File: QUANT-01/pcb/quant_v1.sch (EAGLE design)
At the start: 34 parts, among them SW1 SUBMINI_SPDT, SW2 SUBMINI_SPDT, SW3 SUBMINI_SPDT, SW4 SUBMINI_SPDT

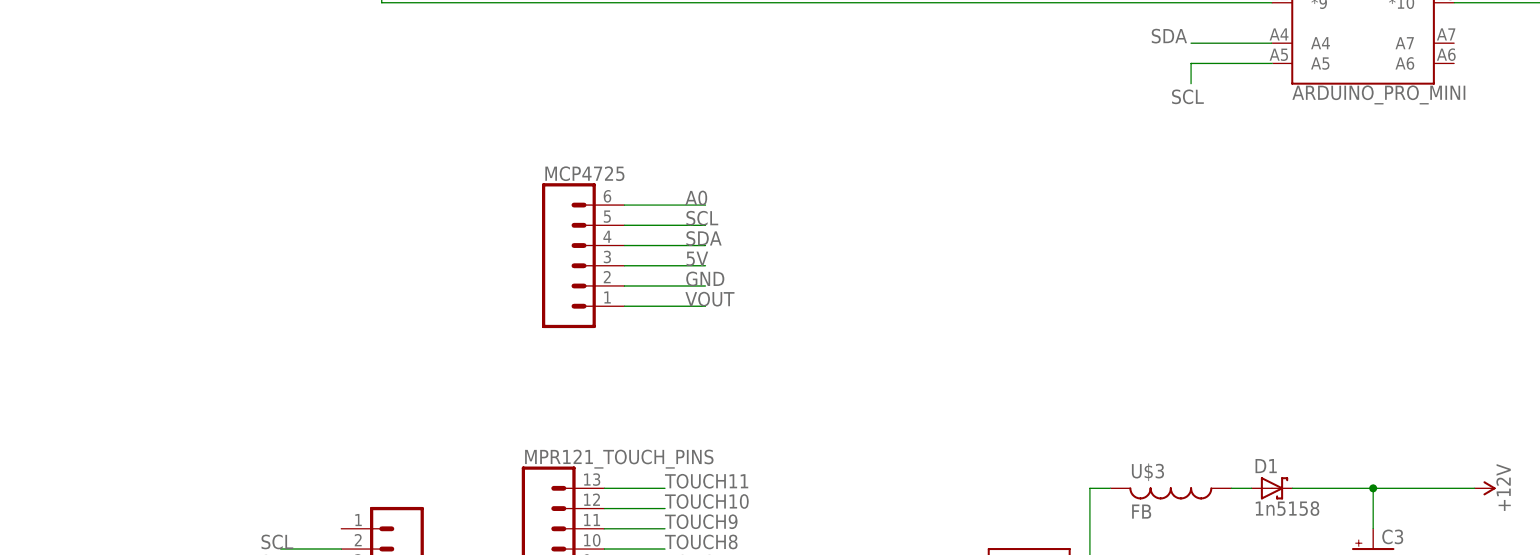
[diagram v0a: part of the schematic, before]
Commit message: added simple GATE out code.
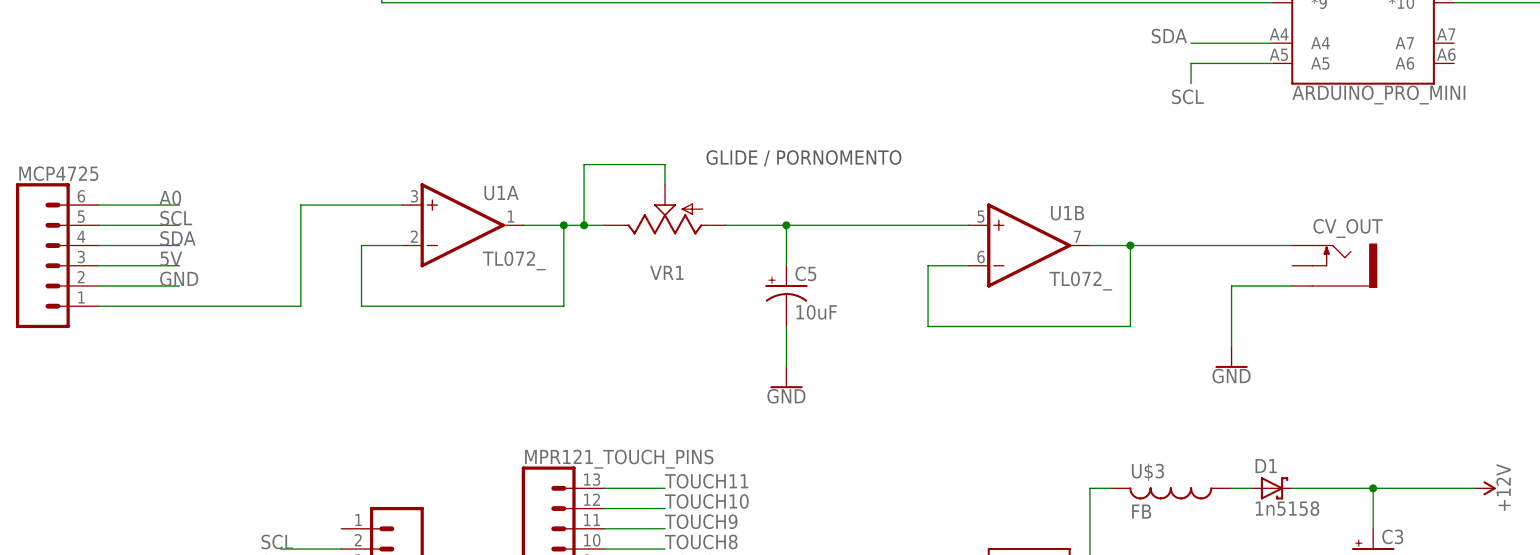
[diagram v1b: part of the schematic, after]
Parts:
- added C5: 10uF, SparkFun-Capacitors:10UF-POLAR-RADIAL-2.5MM-25V-20%
- added CV_OUT: THONKICONNNEW, MusicThingModular:THONKICONNNEW
- added U1: TL072_, MusicThingModular:TL072_
- added VR1: (no value), MusicThingModular:9MM_SNAP-IN_POT_
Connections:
- removed net VOUT: MCP4725.1
- new net N$20: MCP4725.1, U1A.+IN
- new net N$21: U1A.-IN, U1A.OUT, VR1.E, VR1.S
- new net N$23: C5.+, U1B.+IN, VR1.A
- new net N$25: CV_OUT.TIP, U1B.-IN, U1B.OUT
- net GND: now also C5.-, CV_OUT.SLEEVE
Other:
- note added: "GLIDE / PORNOMENTO"
- moved on the sheet: MCP4725
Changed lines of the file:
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@@
 <part name="GND7" library="SparkFun-PowerSymbols" library_urn="urn:adsk.eagle:library:530" deviceset="GND" device=""/>
 <part name="+12V2" library="SparkFun-PowerSymbols" library_urn="urn:adsk.eagle:library:530" deviceset="5V" device="" value="+12V"/>
+<part name="VR1" library="MusicThingModular" deviceset="9MM_SNAP-IN_POT" device="_"/>
+<part name="U1" library="MusicThingModular" deviceset="TL072" device="_"/>
+<part name="C5" library="SparkFun-Capacitors" deviceset="10UF-POLAR" device="-RADIAL-2.5MM-25V-20%" value="10uF"/>
+<part name="GND8" library="SparkFun-PowerSymbols" library_urn="urn:adsk.eagle:library:530" deviceset="GND" device=""/>
+<part name="CV_OUT" library="MusicThingModular" deviceset="THONKICONN" device="NEW"/>
+<part name="GND9" library="SparkFun-PowerSymbols" library_urn="urn:adsk.eagle:library:530" deviceset="GND" device=""/>
 </parts>
 <sheets>
@@
 QUANT_V1
 2018</text>
+<text x="-114.3" y="-25.4" size="1.778" layer="97">GLIDE / PORNOMENTO</text>
 </plain>
 <instances>
@@
 <instance part="GND" gate="1" x="-58.42" y="20.32" rot="R270"/>
 <instance part="SUPPLY1" gate="G$1" x="-12.7" y="12.7" rot="R270"/>
-<instance part="MCP4725" gate="G$1" x="-129.54" y="-38.1"/>
+<instance part="MCP4725" gate="G$1" x="-195.58" y="-38.1"/>
 <instance part="MPR121_TOUCH_PINS" gate="G$1" x="-137.16" y="-81.28"/>
 <instance part="MPR121" gate="G$1" x="-154.94" y="-76.2" rot="R180"/>
@@
 <instance part="GND7" gate="1" x="-170.18" y="43.18" rot="R270"/>
 <instance part="+12V2" gate="G$1" x="-7.62" y="30.48"/>
+<instance part="VR1" gate="G$1" x="-119.38" y="-33.02" rot="R90"/>
+<instance part="U1" gate="A" x="-144.78" y="-33.02"/>
+<instance part="U1" gate="B" x="-73.66" y="-35.56"/>
+<instance part="C5" gate="G$1" x="-104.14" y="-40.64"/>
+<instance part="GND8" gate="1" x="-104.14" y="-53.34"/>
+<instance part="CV_OUT" gate="G$1" x="-35.56" y="-38.1"/>
+<instance part="GND9" gate="1" x="-48.26" y="-50.8"/>
 </instances>
 <busses>
@@
 <segment>
 <pinref part="MCP4725" gate="G$1" pin="4"/>
-<wire x1="-124.46" y1="-35.56" x2="-114.3" y2="-35.56" width="0.1524" layer="91"/>
-<label x="-116.84" y="-35.56" size="1.778" layer="95"/>
+<wire x1="-190.5" y1="-35.56" x2="-180.34" y2="-35.56" width="0.1524" layer="91"/>
+<label x="-182.88" y="-35.56" size="1.778" layer="95"/>
 </segment>
 <segment>
@@
 <segment>
 <pinref part="MCP4725" gate="G$1" pin="5"/>
-<wire x1="-124.46" y1="-33.02" x2="-114.3" y2="-33.02" width="0.1524" layer="91"/>
-<label x="-116.84" y="-33.02" size="1.778" layer="95"/>
+<wire x1="-190.5" y1="-33.02" x2="-180.34" y2="-33.02" width="0.1524" layer="91"/>
+<label x="-182.88" y="-33.02" size="1.778" layer="95"/>
 </segment>
 <segment>
@@
 <segment>
 <pinref part="MCP4725" gate="G$1" pin="3"/>
-<wire x1="-124.46" y1="-38.1" x2="-114.3" y2="-38.1" width="0.1524" layer="91"/>
-<label x="-116.84" y="-38.1" size="1.778" layer="95"/>
+<wire x1="-190.5" y1="-38.1" x2="-180.34" y2="-38.1" width="0.1524" layer="91"/>
+<label x="-182.88" y="-38.1" size="1.778" layer="95"/>
 </segment>
 <segment>
@@
 <segment>
 <pinref part="MCP4725" gate="G$1" pin="2"/>
-<wire x1="-124.46" y1="-40.64" x2="-114.3" y2="-40.64" width="0.1524" layer="91"/>
-<label x="-116.84" y="-40.64" size="1.778" layer="95"/>
+<wire x1="-190.5" y1="-40.64" x2="-180.34" y2="-40.64" width="0.1524" layer="91"/>
+<label x="-182.88" y="-40.64" size="1.778" layer="95"/>
 </segment>
 <segment>
@@
 <wire x1="-93.98" y1="35.56" x2="-93.98" y2="43.18" width="0.1524" layer="91"/>
 </segment>
+<segment>
+<pinref part="C5" gate="G$1" pin="-"/>
+<pinref part="GND8" gate="1" pin="GND"/>
+<wire x1="-104.14" y1="-45.72" x2="-104.14" y2="-50.8" width="0.1524" layer="91"/>
+</segment>
+<segment>
+<pinref part="CV_OUT" gate="G$1" pin="SLEEVE"/>
+<wire x1="-40.64" y1="-40.64" x2="-48.26" y2="-40.64" width="0.1524" layer="91"/>
+<pinref part="GND9" gate="1" pin="GND"/>
+<wire x1="-48.26" y1="-40.64" x2="-48.26" y2="-48.26" width="0.1524" layer="91"/>
+</segment>
 </net>
 <net name="A0" class="0">
 <segment>
 <pinref part="MCP4725" gate="G$1" pin="6"/>
-<wire x1="-124.46" y1="-30.48" x2="-114.3" y2="-30.48" width="0.1524" layer="91"/>
-<label x="-116.84" y="-30.48" size="1.778" layer="95"/>
-</segment>
-</net>
-<net name="VOUT" class="0">
-<segment>
-<pinref part="MCP4725" gate="G$1" pin="1"/>
-<wire x1="-124.46" y1="-43.18" x2="-114.3" y2="-43.18" width="0.1524" layer="91"/>
-<label x="-116.84" y="-43.18" size="1.778" layer="95"/>
+<wire x1="-190.5" y1="-30.48" x2="-180.34" y2="-30.48" width="0.1524" layer="91"/>
+<label x="-182.88" y="-30.48" size="1.778" layer="95"/>
 </segment>
 </net>
@@
 </segment>
 </net>
+<net name="N$20" class="0">
+<segment>
+<pinref part="MCP4725" gate="G$1" pin="1"/>
+<wire x1="-190.5" y1="-43.18" x2="-165.1" y2="-43.18" width="0.1524" layer="91"/>
+<wire x1="-165.1" y1="-43.18" x2="-165.1" y2="-30.48" width="0.1524" layer="91"/>
+<pinref part="U1" gate="A" pin="+IN"/>
+<wire x1="-165.1" y1="-30.48" x2="-152.4" y2="-30.48" width="0.1524" layer="91"/>
+</segment>
+</net>
+<net name="N$21" class="0">
+<segment>
+<pinref part="U1" gate="A" pin="OUT"/>
+<pinref part="VR1" gate="G$1" pin="E"/>
+<wire x1="-137.16" y1="-33.02" x2="-132.08" y2="-33.02" width="0.1524" layer="91"/>
+<junction x="-129.54" y="-33.02"/>
+<wire x1="-132.08" y1="-33.02" x2="-129.54" y2="-33.02" width="0.1524" layer="91"/>
+<wire x1="-129.54" y1="-33.02" x2="-127" y2="-33.02" width="0.1524" layer="91"/>
+<pinref part="VR1" gate="G$1" pin="S"/>
+<wire x1="-119.38" y1="-27.94" x2="-119.38" y2="-25.4" width="0.1524" layer="91"/>
+<wire x1="-119.38" y1="-25.4" x2="-129.54" y2="-25.4" width="0.1524" layer="91"/>
+<wire x1="-129.54" y1="-25.4" x2="-129.54" y2="-33.02" width="0.1524" layer="91"/>
+<junction x="-132.08" y="-33.02"/>
+<pinref part="U1" gate="A" pin="-IN"/>
+<wire x1="-152.4" y1="-35.56" x2="-157.48" y2="-35.56" width="0.1524" layer="91"/>
+<wire x1="-157.48" y1="-35.56" x2="-157.48" y2="-43.18" width="0.1524" layer="91"/>
+<wire x1="-157.48" y1="-43.18" x2="-132.08" y2="-43.18" width="0.1524" layer="91"/>
+<wire x1="-132.08" y1="-43.18" x2="-132.08" y2="-33.02" width="0.1524" layer="91"/>
+</segment>
+</net>
+<net name="N$23" class="0">
+<segment>
+<pinref part="VR1" gate="G$1" pin="A"/>
+<pinref part="U1" gate="B" pin="+IN"/>
+<wire x1="-111.76" y1="-33.02" x2="-104.14" y2="-33.02" width="0.1524" layer="91"/>
+<junction x="-104.14" y="-33.02"/>
+<wire x1="-104.14" y1="-33.02" x2="-81.28" y2="-33.02" width="0.1524" layer="91"/>
+<pinref part="C5" gate="G$1" pin="+"/>
+<wire x1="-104.14" y1="-38.1" x2="-104.14" y2="-33.02" width="0.1524" layer="91"/>
+</segment>
+</net>
+<net name="N$25" class="0">
+<segment>
+<pinref part="U1" gate="B" pin="OUT"/>
+<pinref part="CV_OUT" gate="G$1" pin="TIP"/>
+<wire x1="-66.04" y1="-35.56" x2="-60.96" y2="-35.56" width="0.1524" layer="91"/>
+<junction x="-60.96" y="-35.56"/>
+<wire x1="-60.96" y1="-35.56" x2="-40.64" y2="-35.56" width="0.1524" layer="91"/>
+<pinref part="U1" gate="B" pin="-IN"/>
+<wire x1="-81.28" y1="-38.1" x2="-86.36" y2="-38.1" width="0.1524" layer="91"/>
+<wire x1="-86.36" y1="-38.1" x2="-86.36" y2="-45.72" width="0.1524" layer="91"/>
+<wire x1="-86.36" y1="-45.72" x2="-60.96" y2="-45.72" width="0.1524" layer="91"/>
+<wire x1="-60.96" y1="-45.72" x2="-60.96" y2="-35.56" width="0.1524" layer="91"/>
+</segment>
+</net>

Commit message: started building board.
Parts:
- removed U1: TL072_, MusicThingModular:TL072_
- added C7: 47pf, SparkFun-Capacitors:10NF-PTH-10MM-10000V-1-%
- added C8, C9: 100nf, SparkFun-Capacitors:10NF-PTH-10MM-10000V-1-%
- added CV_INPUT: THONKICONNNEW, MusicThingModular:THONKICONNNEW
- added D11: (no value), SparkFun-LED:LED3MM
- added GATE_OUT: GATE_OUT, MusicThingModular:THONKICONNNEW
- added R10, R11, R17, R18, R9: 100k, SparkFun-Resistors:1KOHM-HORIZ-1/4W-5%
- added R12: 49.9k, SparkFun-Resistors:1KOHM-HORIZ-1/4W-5%
- added R13, R19, R20: 10k, SparkFun-Resistors:1KOHM-HORIZ-1/4W-5%
- added R14, R21: 1k, SparkFun-Resistors:1KOHM-HORIZ-1/4W-5%
- added SW5_MODE: SUBMINI_SPDT, MusicThingModular:SUBMINI_SPDT
- added U3: MCP6002, MusicThingModular:TL072_
- added U4: TL074_, MusicThingModular:TL074_
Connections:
- new net N$22: CV_INPUT.TIP, R9.1
- new net N$24: R10.2, R9.2, U4A.-IN
- new net N$26: B1.A1, R13.2
- new net N$27: R13.1, SW5_MODE.COMMON
- new net N$28: R10.1, R11.2, U4A.OUT
- new net N$29: R11.1, R12.2, U3A.-IN
- new net N$30: R17.1, R18.1, U3B.+IN
- new net N$31: GATE_OUT.TIP, R21.1
- new net N$32: R14.2, U4D.-IN
- new net N$33: D11.A, R14.1, U4D.OUT
- new net N$37: B1.A2, R20.2, U4D.+IN
- new net N$38: C7.2, R19.2, R20.1, U3B.-IN
- new net N$39: C7.1, R19.1, R21.2, U3B.OUT
- new net VEE: B1.A0, R12.1, U3A.OUT
- net 5V: now also C8.1, C9.1, R17.2, U3P.V+, U4P.V+, U4P.V-
- net GND: now also C8.2, C9.2, CV_INPUT.SLEEVE, D11.C, GATE_OUT.SLEEVE, R18.2, SW5_MODE.O, U3A.+IN, U3P.V-, U4A.+IN
- net N$20: now also U4B.+IN; no longer U1A.+IN
- net N$21: now also U4B.-IN, U4B.OUT; no longer U1A.-IN, U1A.OUT
- net N$23: now also U4C.+IN; no longer U1B.+IN
- net N$25: now also U4C.-IN, U4C.OUT; no longer U1B.-IN, U1B.OUT
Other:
- note added: "GATE INDICATOR"
- note added: "gate signal"
- moved on the sheet: SW1, SW2, SW3, SW4

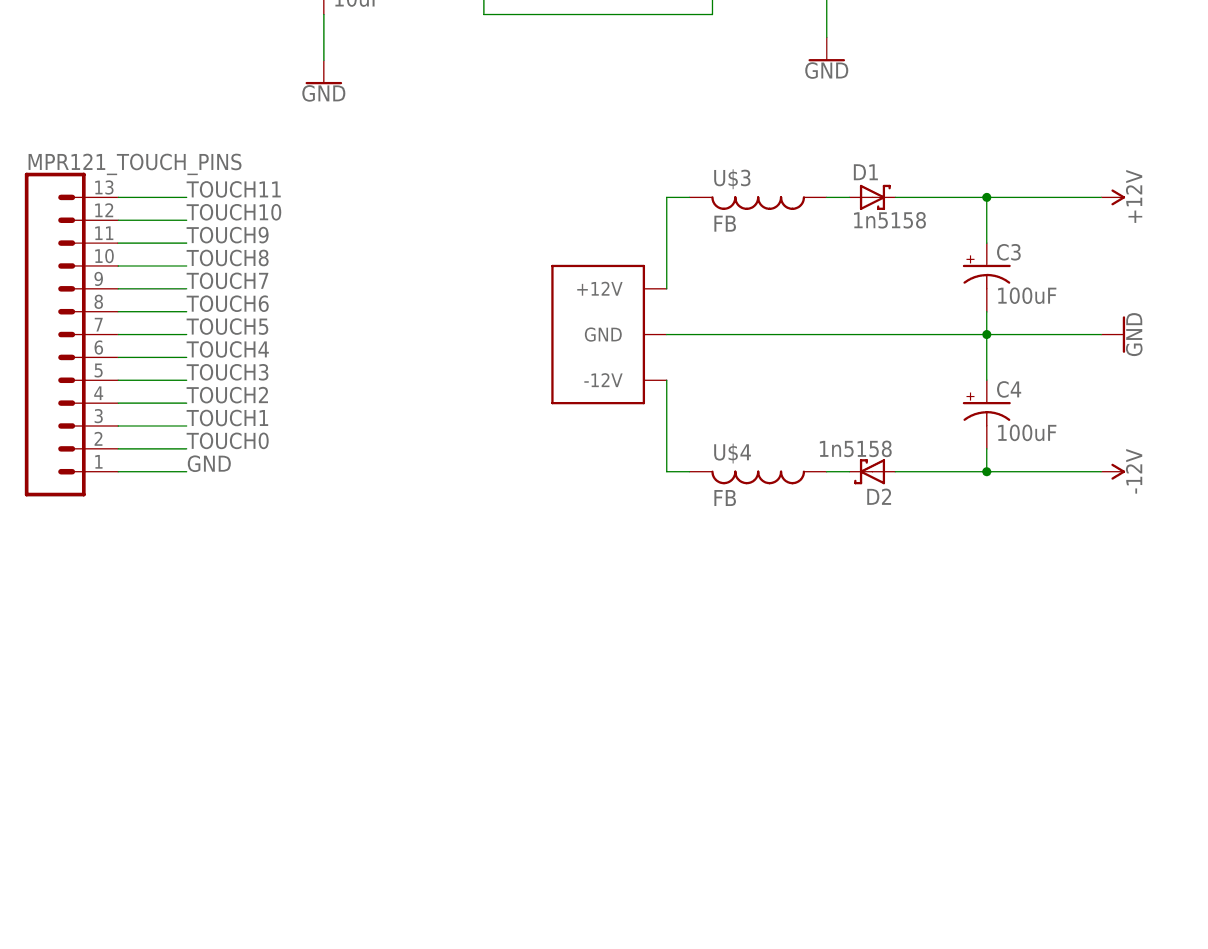
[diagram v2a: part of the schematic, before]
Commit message: got bottom pcb basic layout in place.
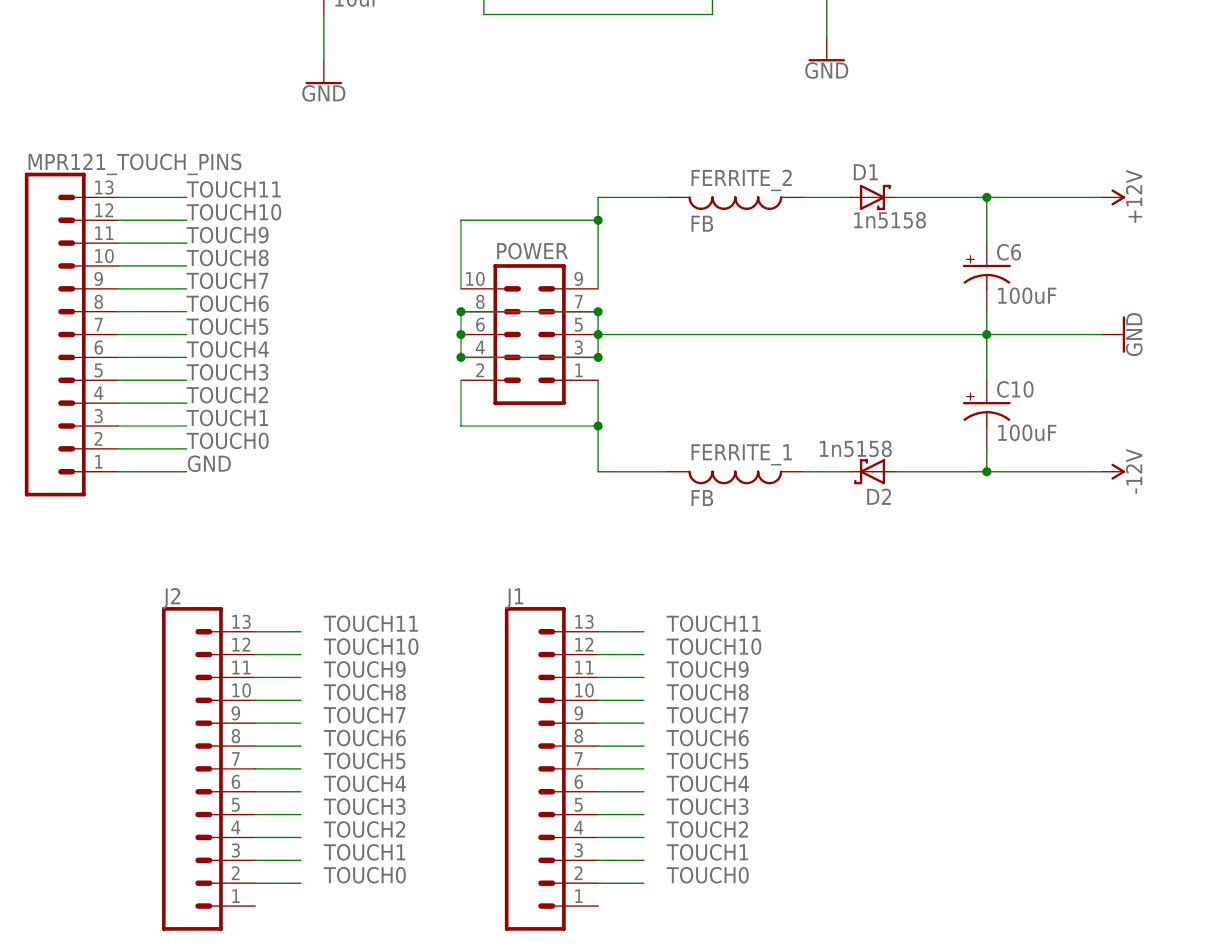
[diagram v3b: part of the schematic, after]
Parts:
- removed C3, C4: 100uF, SparkFun-Capacitors:1000UF-RADIAL-5MM-25V-20%
- removed U$1: EURO_POWER_LOCK, MusicThingModular:EURO_POWER_LOCK
- removed U$3, U$4: FB, adafruit:FB
- added C10, C6: 100uF, SparkFun-Capacitors:100UF-POLAR-RADIAL-2.5MM-25V-20%
- added FERRITE_1, FERRITE_2: FB, adafruit:FB
- added J1, J2: (no value), SparkFun-Connectors:CONN_13
- added POWER: EURO_POWER_HEADERREGULAR, MusicThingModular:EURO_POWER_HEADERREGULAR
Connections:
- removed net -12V: U$1.-12V, U$4.2
- new net N$34: FERRITE_1.2, POWER.1, POWER.2
- net 5V: now also C10.-, C6.+; no longer C3.+, C4.-
- net GND: now also C10.+, C6.-, POWER.3, POWER.4, POWER.5, POWER.6, POWER.7, POWER.8; no longer C3.-, C4.+, U$1.GND
- net N$1: now also FERRITE_2.2, POWER.10, POWER.9; no longer U$1.+12V, U$3.2
- net N$2: now also FERRITE_1.1; no longer U$4.1
- net N$3: now also FERRITE_2.1; no longer U$3.1
- net TOUCH0: now also J1.2, J2.2
- net TOUCH1: now also J1.3, J2.3
- net TOUCH10: now also J1.12, J2.12
- net TOUCH11: now also J1.13, J2.13
- net TOUCH2: now also J1.4, J2.4
- net TOUCH3: now also J1.5, J2.5
- net TOUCH4: now also J1.6, J2.6
- net TOUCH5: now also J1.7, J2.7
- net TOUCH6: now also J1.8, J2.8
- net TOUCH7: now also J1.9, J2.9
- net TOUCH8: now also J1.10, J2.10
- net TOUCH9: now also J1.11, J2.11

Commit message: started wiring.
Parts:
- added J3, J4, J5, J6: (no value), SparkFun-Connectors:CONN_09
- added R15, R16, R22, R23: 10k, SparkFun-Resistors:1KOHM-HORIZ-1/4W-5%
- CV_OUT: value THONKICONNNEW -> CV_OUT
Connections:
- net N$21 renamed GLIDE_WIPER
- net N$23 renamed GLIDE_1
- removed net N$26: B1.A1, R13.2
- removed net N$33: D11.A, R14.1, U4D.OUT
- removed net VEE: B1.A0, R12.1, U3A.OUT
- new net -12V: U4P.V-
- new net CV_IN: B1.A1, J5.4, R12.1, U3A.OUT
- new net CV_INPUT: R9.1
- new net CV_OUT: J5.2, U4C.-IN, U4C.OUT
- new net GATE_LED: J5.1, R14.1, U4D.OUT
- new net GATE_OUT: J5.3, R21.1
- new net LED_I: B1.*9, J3.1, J4.1, R1.2
- new net LED_II: B1.8, J3.2, J4.2, R2.2
- new net LED_III: B1.7, J3.3, J4.3, R3.2
- new net LED_IV: B1.*6, J3.4, J4.4, R4.2
- new net LED_V: B1.*5, J3.5, J4.5, R5.2
- new net LED_VI: B1.4, J3.6, J4.6, R6.2
- new net LED_VII: B1.*3, J3.7, J4.7, R7.2
- new net LED_VIII: B1.2, J3.8, J4.8, R8.2
- new net N$21: GATE_OUT.TIP, J6.3
- new net N$23: D11.A, J6.1
- new net SW_MODE: B1.A0, J5.5
- net +12V: now also B1.RAW, C6.+, C9.1, D1.C, U4P.V+
- net 5V: now also J1.1, J2.1; no longer B1.RAW, C6.+, C9.1, D1.C, U4P.V+, U4P.V-
- net GND: now also J3.9, J4.9; no longer MPR121_TOUCH_PINS.1
- net N$10: now also CV_INPUT.TIP, J6.4; no longer B1.7, R6.2
- net N$11: now also J6.7, R16.2; no longer B1.8, R7.2
- net N$12: now also J6.6, R15.2; no longer B1.*9, R8.2
- net N$22: now also CV_OUT.TIP, J6.2; no longer CV_INPUT.TIP, R9.1
- net N$25: now also J6.8, R22.2; no longer CV_OUT.TIP, U4C.-IN, U4C.OUT
- net N$31: now also J6.5, R13.2; no longer GATE_OUT.TIP, R21.1
- net N$4: now also R23.1, SW1.COMMON; no longer B1.2, R1.2
- net N$6: now also R22.1, SW2.COMMON; no longer B1.*3, R2.2
- net N$7: now also R16.1, SW3.COMMON; no longer B1.4, R3.2
- net N$8: now also R15.1, SW4.COMMON; no longer B1.*5, R4.2
- net N$9: now also J6.9, R23.2; no longer B1.*6, R5.2
- net SW1: now also J5.9; no longer SW4.COMMON
- net SW2: now also J5.8; no longer SW3.COMMON
- net SW3: now also J5.7; no longer SW2.COMMON
- net SW4: now also J5.6; no longer SW1.COMMON
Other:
- moved on the sheet: C10, C5, C6, CV_INPUT, CV_OUT, D1, D10, D11, D2, D3, D4, D5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
